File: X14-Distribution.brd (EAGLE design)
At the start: 152.4 x 76.2 mm, 57 parts, among them Q1 310mA/60V/1.6Ω, Q2 IRF1018EPBF, Q3 IRF1018EPBF, Q4 IRF1018EPBF, Q5 IRLML5203, Q6 IRLML5203, Q7 IRLML5203, Q8 IRLML5203, U1 DIST_OR_CONTROL_ALTMK06A-M, U2 DIST_OR_CONTROL_ALTMK06A-M

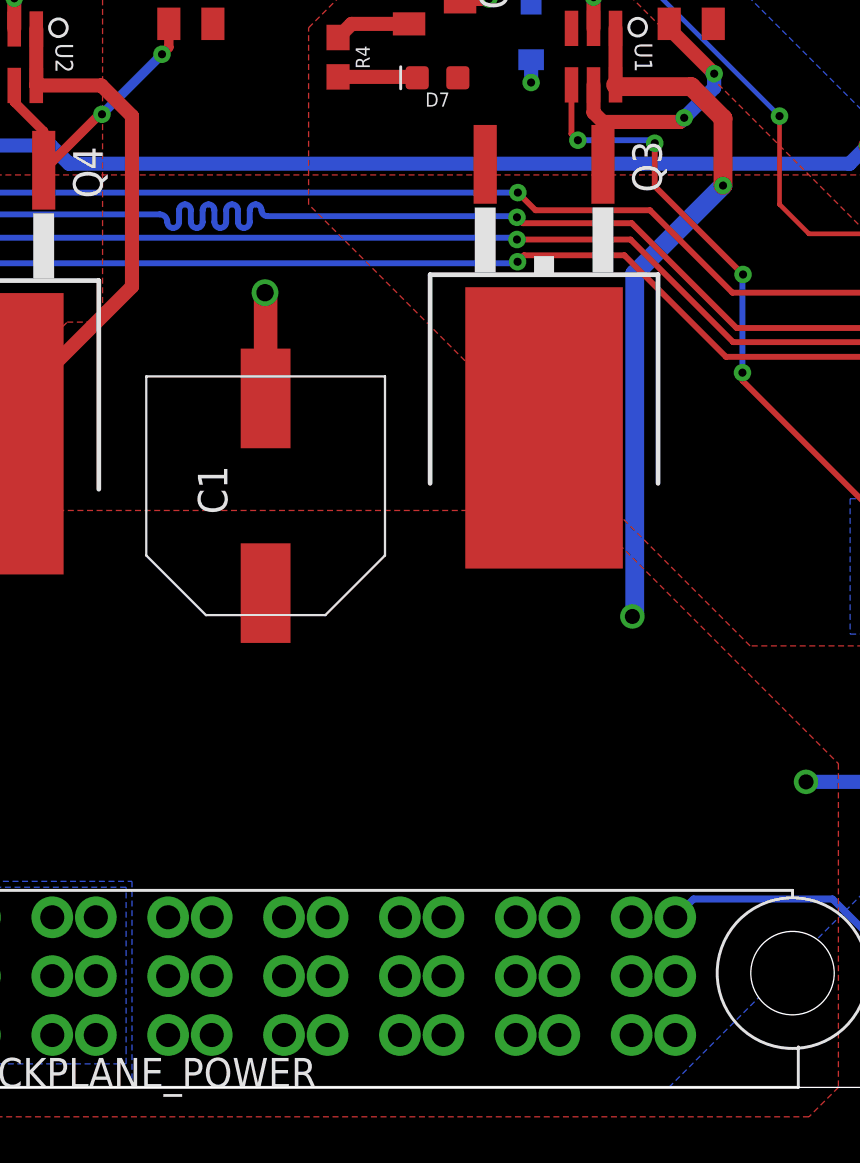
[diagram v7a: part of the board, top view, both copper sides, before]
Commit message: Finished all design review changes, except bricks connector
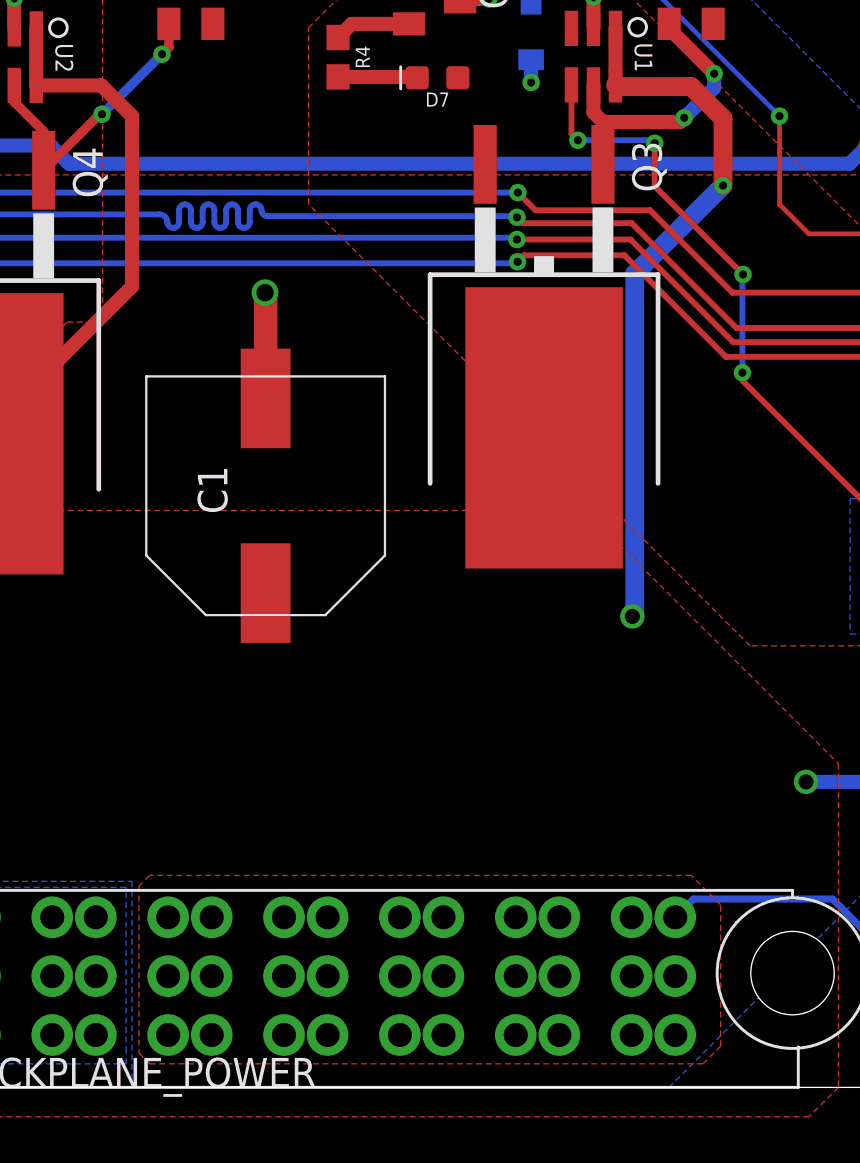
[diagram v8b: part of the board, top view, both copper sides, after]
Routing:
- net OR_DRIVE_A: track 13.4 -> 12.6 mm
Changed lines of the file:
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@@
 <contactref element="Q3" pad="1"/>
 <contactref element="Q5" pad="1"/>
-<wire x1="96.52" y1="40.588" x2="96.52" y2="39.826" width="0.6096" layer="1"/>
-<wire x1="96.52" y1="40.588" x2="96.4946" y2="40.6134" width="0.6096" layer="1"/>
 <via x="100.0252" y="41.8338" extent="1-16" drill="0.35"/>
 <wire x1="100.0252" y1="41.8338" x2="101.3206" y2="43.1292" width="0.6096" layer="16"/>
@@
 <vertex x="44.45" y="32.258"/>
 </polygon>
-</signal>
+<polygon width="0.254" layer="1" pour="cutout">
+<vertex x="76.5048" y="8.6868"/>
+<vertex x="76.5048" y="1.4732"/>
+<vertex x="76.962" y="1.016"/>
+<vertex x="100.838" y="1.016"/>
+<vertex x="101.6" y="1.778"/>
+<vertex x="101.6" y="7.874"/>
+<vertex x="100.33" y="9.144"/>
+<vertex x="76.962" y="9.144"/>
+</polygon>
+</signal>
